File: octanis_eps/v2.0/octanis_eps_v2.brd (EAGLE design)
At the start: 95 x 50 mm, 187 parts, among them Q1 CSD16327Q3_DQG_8, Q2 CSD16327Q3_DQG_8, Q3 CSD16327Q3_DQG_8, Q4 BSS123, Q5 CSD16327Q3_DQG_8, Q6 CSD16327Q3_DQG_8, Q7 BSC0901NS, U1 MSP430FR5969, U10 INA213, U11 MIC5019, U12 TPS61088, U13 TPS61232, U15 Value, U16 Value, U17 Value, U2 OPA2333DGK, U3 TPS2022D, U4 TPS2022D, U5 BQ24650_RVA_16, U7 TPS61232, U9 INA213, X1 32.768kHz

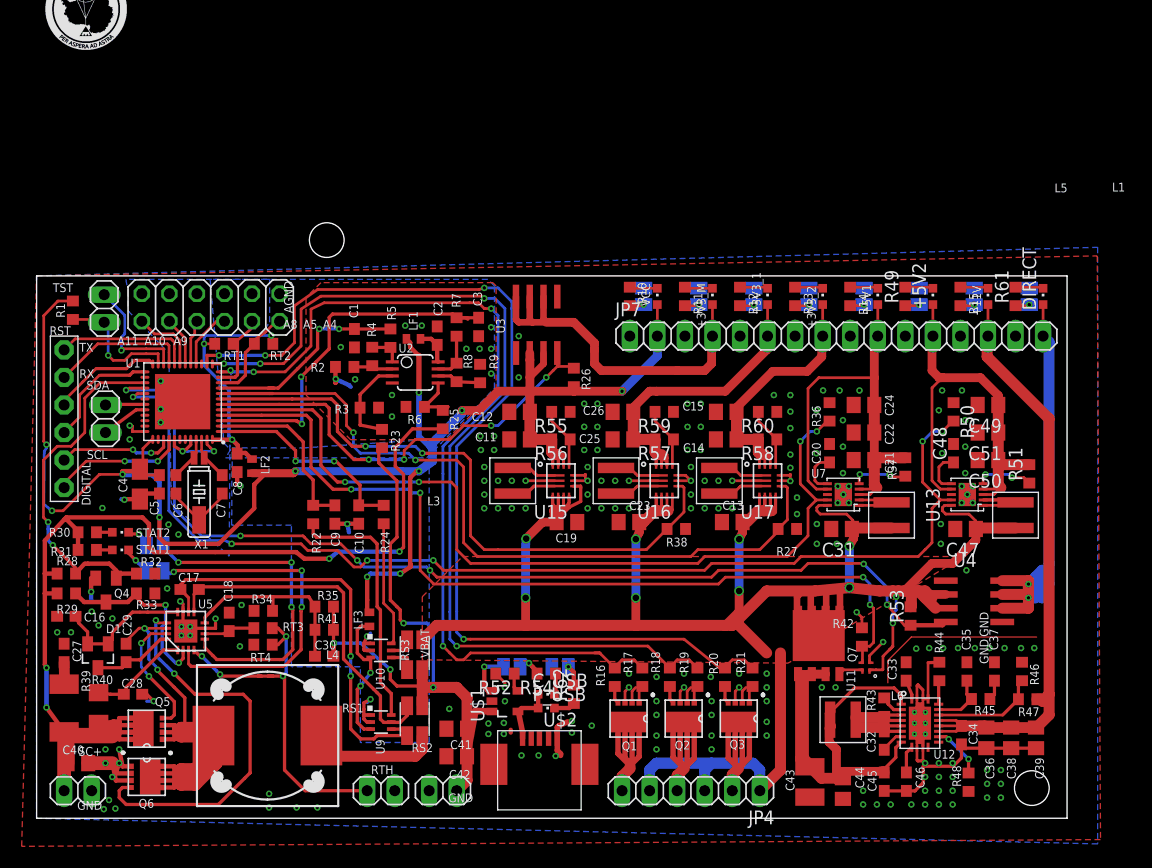
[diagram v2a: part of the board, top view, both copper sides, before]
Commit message: corrected some GND mistakes; finished v2.0 silk layer
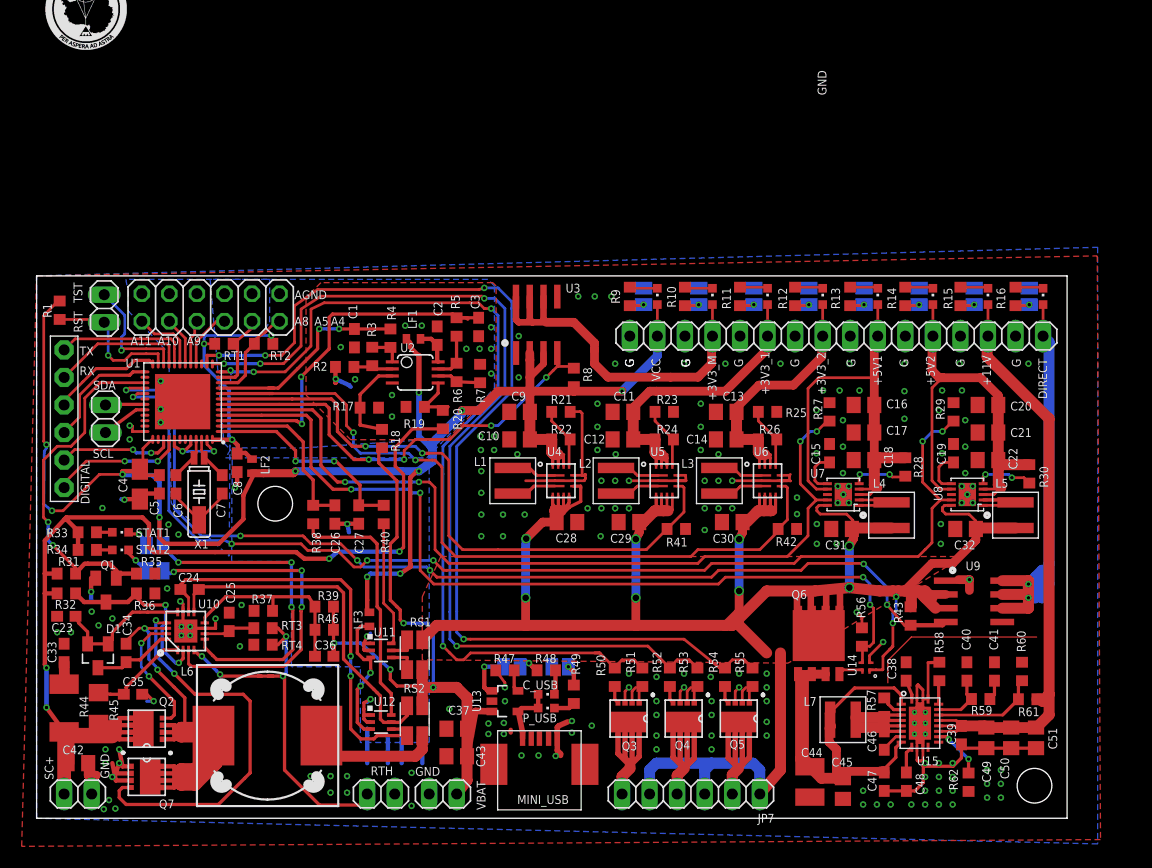
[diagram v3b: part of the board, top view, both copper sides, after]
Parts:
- removed J1, J2, J3, J4: (no value), jumper:SJ
- removed RS3: 10m, Octanis1_EPS:4PADS_RESISTOR
- removed U$1: MCP73831/2, Octanis1_EPS:SOT23-5
- removed U16: Value, octanis_eps_v05:RNC0014A
- added J108, J109, J110, J111: (no value), jumper:SJ
- added RS2: 10m, Octanis1_EPS:4PADS_RESISTOR
- added U14: MIC5019, Octanis1_EPS:QFN-4
- added U8: TPS61232, texasinstruments:S-PVSON-N10
- C10, C9: value 1.5uF -> 22uF; device rcl:C0603 -> resistor:C0805
- C13: value 10uF -> 22uF
- C15: value 22uF -> 10nF; device resistor:C0805 -> rcl:C0603
- C16, C18: value 1uF -> 22uF; device rcl:C0603 -> resistor:C0805
- C17, C32: value 100nF -> 22uF; device rcl:C0603 -> resistor:C0805
- C19: value 10uF -> 10nF; device resistor:C0805 -> rcl:C0603
- C20: value 10nF -> 22uF; device rcl:C0603 -> resistor:C0805
- C23: value 10uF -> 1uF; device resistor:C0805 -> rcl:C0603
- C24, C47: value 22uF -> 100nF; device resistor:C0805 -> rcl:C0603
- C25, C39: value 22uF -> 1uF; device resistor:C0805 -> rcl:C0603
- C26: value 22uF -> 1.5uF; device resistor:C0805 -> rcl:C0603
- C27: value 2.2uF -> 1.5uF
- C28: value 1uF -> 10uF; device rcl:C0603 -> resistor:C0805
- C29, C45: value 100nF -> 10uF; device rcl:C0603 -> resistor:C0805
- C30: value 22pF -> 10uF; device rcl:C0603 -> resistor:C0805
- C34: value 1uF -> 100nF
- C35: value 150pF -> 1uF
- C36: value 22uF -> 22pF; device resistor:C0805 -> rcl:C0603
- C37: value 4.7nF -> 10uF; device rcl:C0603 -> resistor:C0805
- C38: value 22uF -> 2.2uF; device resistor:C0805 -> rcl:C0603
- C40: value 10uF -> 150pF; device resistor:C0805 -> rcl:C0603
- C41: value 10uF -> 4.7nF; device resistor:C0805 -> rcl:C0603
- C43: value 47uF Tantal -> 10uF; device rcl:C1210 -> resistor:C0805
- C44: value 10uF -> 47uF Tantal; device resistor:C0805 -> rcl:C1210
- C46: value 47nF -> 100nF
- C48: value 10nF -> 47nF
- JP3: device Headerlibrary:1X02 -> Headerlibrary:1X16
- JP4: device Headerlibrary:1X06 -> Headerlibrary:1X02
- JP7: device Headerlibrary:1X16 -> Headerlibrary:1X06
- L4: value DR127_6u8 -> 1uH; device inductors:DR127 -> Coilcraft:XFL4020
- L6: value 1.5uH -> DR127_6u8; device Coilcraft:XFL4020 -> inductors:DR127
- L7: value 1uH -> 1.5uH
- Q1: value CSD16327Q3_DQG_8 -> BSS123; device texasinstruments:DQG8 -> transistor-small-signal:SOT23
- Q4: value BSS123 -> CSD16327Q3_DQG_8; device transistor-small-signal:SOT23 -> texasinstruments:DQG8
- Q6: value CSD16327Q3_DQG_8 -> BSC0901NS; device texasinstruments:DQG8 -> transistor-power:PG-TDSON-8
- Q7: value BSC0901NS -> CSD16327Q3_DQG_8; device transistor-power:PG-TDSON-8 -> texasinstruments:DQG8
- R13, R16: value 1k -> 1.5k
- R17, R19: value 1M -> 100k (0.1%)
- R18: value 1k -> 200k (0.1%)
- R20, R7: value 1k -> 330k (0.1%)
- R21: value 1M -> 150k
- R22, R24: value 1k -> 360k
- R23: value 200k (0.1%) -> 150k
- R25: value 330k (0.1%) -> 150k
- R26: value 1M -> 360k; device resistor:R0603 -> rcl:R0603
- R27, R53: device resistor:R0603 -> rcl:R0603
- R28: value dnp -> 1M
- R29: value Rmpph -> 1M
- R30: value 4k7 -> 1M
- R31: value 4k7 -> dnp
- R32: value 1M -> Rmpph
- R33: value Rmppl -> 4k7
- R34: value 100k (1%) -> 4k7
- R35: value 100k (1%) -> 1M
- R36: value 1M -> Rmppl
- R37: value 1M -> 100k (1%)
- R38: value 1M -> 1k; device resistor:R0603 -> rcl:R0603
- R39: value 2 -> 100k (1%); device rcl:R2010 -> rcl:R0603
- R4: value 100k (0.1%) -> 1k
- R40: value 10 -> 1k; device rcl:R1206 -> rcl:R0603
- R41: value 2.2M (1%) -> 1M; device rcl:R0603 -> resistor:R0603
- R42: device rcl:R0603 -> resistor:R0603
- R43: value 47k -> 1M
- R44: value 100k -> 2; device resistor:R0603 -> rcl:R2010
- R45: value 150-220k -> 10; device resistor:R0603 -> rcl:R1206
- R46: value 56k -> 2.2M (1%); device resistor:R0603 -> rcl:R0603
- R47: value 430k -> 2k; device resistor:R0603 -> rcl:R0603
- R48: value dnp -> 470; device resistor:R0603 -> rcl:R0603
- R49: value 1.5k -> 1k
- R50: value 1M -> 1k
- R52: value 2k -> 1k
- R54: value 470 -> 1k
- R55: value 150k -> 1M
- R56: value 360k -> 1M
- R57: value 360k -> 47k; device rcl:R0603 -> resistor:R0603
- R58: value 360k -> 100k; device rcl:R0603 -> resistor:R0603
- R59: value 150k -> 150-220k; device rcl:R0603 -> resistor:R0603
- R60: value 150k -> 56k; device rcl:R0603 -> resistor:R0603
- R61: value 1.5k -> 430k; device rcl:R0603 -> resistor:R0603
- R62: value 1k -> dnp; device rcl:R0603 -> resistor:R0603
- R8: value 100k (0.1%) -> 1M; device rcl:R0603 -> resistor:R0603
- R9: value 330k (0.1%) -> 1k
- U10: value INA213 -> BQ24650_RVA_16; device Octanis1_EPS:SC70-6 -> octanis_eps_v05:RVA16_2P14X2P14
- U11: value MIC5019 -> INA213; device Octanis1_EPS:QFN-4 -> Octanis1_EPS:SC70-6
- U12: value TPS61088 -> INA213; device texasinstruments:R-PVQFN-N20 -> Octanis1_EPS:SC70-6
- U13: value TPS61232 -> MCP73831/2; device texasinstruments:S-PVSON-N10 -> Octanis1_EPS:SOT23-5
- U15: value Value -> TPS61088; device octanis_eps_v05:RNC0014A -> texasinstruments:R-PVQFN-N20
- U4: value TPS2022D -> Value; device Octanis1_EPS:SO8 -> octanis_eps_v05:RNC0014A
- U5: value BQ24650_RVA_16 -> Value; device octanis_eps_v05:RVA16_2P14X2P14 -> octanis_eps_v05:RNC0014A
- U9: value INA213 -> TPS2022D; device Octanis1_EPS:SC70-6 -> Octanis1_EPS:SO8
- moved R30 87.0 mm to (91.5, 31.8), turned to 90 degrees
- moved R29 83.5 mm to (84.5, 37.5), turned to 270 degrees
- moved C40 82.4 mm to (85.8, 13.5), turned to 90 degrees
- moved R45 81.3 mm to (5.71, 10.2), turned to 90 degrees
- moved R44 80.8 mm to (2.54, 10.2)
- moved J102 79.7 mm to (10.9, 22.8), turned to 0 degrees
- moved R28 78.0 mm to (80.1, 32.4), turned to 90 degrees
- moved C33 77.6 mm to (2.54, 15.2)
- moved C34 77.4 mm to (8.26, 15.2), turned to 270 degrees
- moved C35 76.9 mm to (8.89, 11.4), turned to 0 degrees
- moved C16 76.1 mm to (76.3, 38.1)
- moved J103 69.3 mm to (10.9, 25.1), turned to 0 degrees
- moved JP3 67.8 mm to (73.7, 44.5), turned to 0 degrees
- moved R36 65.2 mm to (10.1, 20.7), turned to 180 degrees
- moved C24 64.5 mm to (14.1, 21.1)
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- renumbered U$2 to MINI_USB, U17 to U6
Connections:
- net +12V: now also C49.2, C50.2, C51.2, JP3.14, R61.2, U15.P$14, U15.P$15, U15.P$16; no longer C34.2, C36.2, C38.2, JP7.14, R47.2, U12.P$14, U12.P$15, U12.P$16
- net +3V3: now also C10.1, C9.1, JP3.2, R22.2, R8.2, U4.12, U4.13, U4.14; no longer C11.1, C12.1, JP7.2, R26.2, R56.2, U15.12, U15.13, U15.14
- net +3V3_1: now also C11.1, C12.1, JP3.6, R24.2, U5.12, U5.13, U5.14; no longer C25.1, C26.1, JP7.6, R57.2, U16.12, U16.13, U16.14
- net +3V3_2: now also C13.1, JP3.8, R26.2; no longer C15.1, JP7.8, R58.2
- net +3V3_M: now also JP3.4; no longer JP7.4
- net +5V_1: now also C16.1, C17.1, C18.1, JP3.10, R28.2; no longer C21.1, C22.1, C24.1, JP7.10, R37.2
- net +5V_2: now also C20.1, C21.1, C22.1, JP3.12, R30.2, U8.3, U8.4, U8.7; no longer C49.1, C50.1, C51.1, JP7.12, R51.2, U13.3, U13.4, U13.7
- net AGND: now also C26.1, C27.1, R17.1, R19.1, R7.2, U11.1, U11.2, U12.1, U12.2; no longer C10.1, C9.1, R3.1, R6.1, R9.2, U10.1, U10.2, U9.1, U9.2
- net AVCC1: now also U11.3, U12.3; no longer U10.3, U9.3
- net BAT+: now also C36.1, C37.1, C43.1, R18.2, R39.2, R46.2, RS1.I1, RS2.I2, U13.3; no longer C30.1, C41.1, C42.1, R23.2, R35.2, R41.2, RS1.I2, RS3.I1, U$1.3
- net BAT_11V: now also C47.1, L7.P$1, Q6.1, Q6.2, Q6.3, U15.P$2, U15.P$9; no longer C43.1, L6.P$1, Q7.1, Q7.2, Q7.3, U12.P$2, U12.P$9
- net BAT_OUT: now also C28.1, C29.1, C30.1, C32.1, JP7.1, JP7.3, JP7.5, L4.P$1, Q6.5, Q6.6, Q6.7, Q6.8, R43.2, RS1.I2, U14.P$1, U14.P1, U4.4, U4.5, U4.6, U4.7, U4.8, U5.4, U5.5, U5.6, U5.7, U8.10, U9.2, U9.3; no longer C13.1, C19.1, C23.1, C47.1, JP4.1, JP4.3, JP4.5, L7.P$1, Q7.5, Q7.6, Q7.7, Q7.8, R53.2, RS3.I2, U11.P$1, U11.P1, U13.10, U15.4, U15.5, U15.6, U15.7, U15.8, U16.4, U16.5, U16.6, U16.7, U4.2, U4.3
- net DIRECT: now also JP3.16, U9.6, U9.7, U9.8; no longer JP7.16, U4.6, U4.7, U4.8
- net EN_12V: now also R56.2, U14.P$3, U14.P3; no longer R42.2, U11.P$3, U11.P3
- net EN_3V3_1: now also R41.1, U5.8; no longer R38.1, U16.8
- net EN_3V3_2: now also R42.1; no longer R27.1
- net EN_3V3_M: now also R8.1; no longer R26.1
- net EN_5V_1: now also R27.2; no longer R36.2
- net EN_5V_2: now also R29.2, U8.9; no longer R50.2, U13.9
- net EN_DIRECT: now also R43.1, U9.4; no longer R53.1, U4.4
- net EN_HEAT1: now also R50.2, R51.1; no longer R16.2, R17.1
- net EN_HEAT2: now also R52.2, R53.1; no longer R18.2, R19.1
- net EN_HEAT3: now also R54.2, R55.1; no longer R20.2, R21.1
- net EN_SC: now also Q1.1, R31.1, R35.2; no longer Q4.1, R28.1, R32.2
- net GND: now also C10.2, C17.2, C29.2, C30.2, C32.2, C38.2, C40.2, C42.1, C49.1, C50.1, C51.1, C9.2, J100.2, J108.1, J109.1, J110.1, J111.1, JP3.1, JP3.11, JP3.13, JP3.15, JP3.3, JP3.5, JP3.7, JP3.9, Q4.1, Q4.3, Q5.1, Q5.2, Q5.3, Q7.1, Q7.2, Q7.3, R21.1, R23.1, R25.1, R27.1, R29.1, R35.1, R37.1, R41.2, R42.2, R47.2, R51.2, R53.2, R55.2, R56.1, R58.1, R62.2, U10.11, U10.17, U10.7, U10.V, U10.V_1, U10.V_2, U10.V_3, U13.2, U14.P$2, U14.P2, U15.P$20, U15.PGND1, U15.PGND10, U15.PGND11, U15.PGND12, U15.PGND2, U15.PGND3, U15.PGND4, U15.PGND5, U15.PGND6, U15.PGND7, U15.PGND8, U15.PGND9, U4.10, U4.2, U4.9, U5.10, U5.2, U5.9, U8.EXPAD, U8.GND1, U8.GND2, U8.GND3, U8.GND4, U8.GND5, U9.1; no longer C24.2, C26.2, C27.2, C34.1, C36.1, C38.1, C40.1, C42.2, C46.2, C49.2, C50.2, C51.2, J1.1, J102.1, J103.1, J3.1, J4.2, JP7.1, JP7.11, JP7.13, JP7.15, JP7.3, JP7.5, JP7.7, JP7.9, Q1.1, Q1.3, Q2.1, Q2.2, Q2.3, Q6.1, Q6.2, Q6.3, R17.2, R19.2, R21.2, R27.2, R32.1, R33.1, R34.1, R38.2, R42.1, R44.1, R46.1, R48.2, R50.1, R52.2, R55.1, R59.1, U$1.2, U11.P$2, U11.P2, U12.P$20, U12.PGND1, U12.PGND10, U12.PGND11, U12.PGND12, U12.PGND2, U12.PGND3, U12.PGND4, U12.PGND5, U12.PGND6, U12.PGND7, U12.PGND8, U12.PGND9, U13.EXPAD, U13.GND1, U13.GND2, U13.GND3, U13.GND4, U13.GND5, U15.10, U15.2, U15.9, U16.10, U16.2, U16.9, U4.1, U5.11, U5.17, U5.7, U5.V, U5.V_1, U5.V_2, U5.V_3
- net HEAT1: now also JP7.6, Q3.5, Q3.6, Q3.7, Q3.8; no longer JP4.6, Q1.5, Q1.6, Q1.7, Q1.8
- net HEAT2: now also JP7.4, Q4.5, Q4.6, Q4.7, Q4.8; no longer JP4.4, Q2.5, Q2.6, Q2.7, Q2.8
- net HEAT3: now also JP7.2, Q5.5, Q5.6, Q5.7, Q5.8; no longer JP4.2, Q3.5, Q3.6, Q3.7, Q3.8
- net I2C_SCL: now also JP4.2; no longer JP3.2
- net I2C_SDA: now also JP4.1; no longer JP3.1
- net IND: now also L4.P$2; no longer L5.P$2
- net IND1: now also L5.P$2, U8.1, U8.2; no longer L7.P$2, U13.1, U13.2
- net I_IN: now also C26.2, R38.1; no longer C9.2, R22.1
- net I_OUT: now also C27.2, R40.1; no longer C10.2, R24.1
- net LED1: now also R14.2; no longer R49.2
- net LED2: now also R16.2; no longer R61.2
- net LED5: now also R13.2; no longer R14.2
- net N$1: now also L1.P$1, U4.3; no longer L3.P$1, U15.3
- net N$10: now also Q6.4, U14.P$4, U14.P4; no longer Q7.4, U11.P$4, U11.P4
- net N$11: now also L3.P$1; no longer L1.P$1
- net N$12: now also L3.P$2; no longer L1.P$2
- net N$14: now also J107.2, R13.1; no longer J103.2, R14.1
- net N$19: now also R3.1, R4.2; no longer R4.1, R5.2
- net N$2: now also R28.1; no longer R37.1
- net N$20: now also R3.2; no longer R4.2
- net N$21: now also R17.2, R18.1; no longer R23.1, R3.2
- net N$22: now also R5.2, R6.1; no longer R7.2, R8.1
- net N$23: now also R6.2, R7.1; no longer R8.2, R9.1
- net N$24: now also R19.2, R20.1; no longer R25.1, R6.2
- net N$25: now also R40.2, U11.6; no longer R24.2, U10.6
- net N$26: now also R38.2, U12.6; no longer R22.2, U9.6
- net N$27: now also Q5.4, R54.1; no longer Q3.4, R20.1
- net N$3: now also L1.P$2, U4.1; no longer L3.P$2, U15.1
- net N$31: now also Q4.4, R52.1; no longer Q2.4, R18.1
- net N$32: now also RS1.V1, U11.4; no longer RS3.V1, U10.4
- net N$33: now also RS1.V2, U11.5; no longer RS3.V2, U10.5
- net N$34: now also R21.2, R22.1, U4.11; no longer R55.2, R56.1, U15.11
- net N$35: now also R23.2, R24.1, U5.11; no longer R57.1, R59.2, U16.11
- net N$37: now also Q3.4, R50.1; no longer Q1.4, R16.1
- net N$38: now also C46.2, U15.P$8; no longer C32.2, U12.P$8
- net N$39: now also R10.2; no longer R11.2
- net N$4: now also L6.2, RS2.I1; no longer L4.2, RS1.I1
- net N$40: now also J110.2, R10.1; no longer J106.2, R11.1
- net N$42: now also C33.1, R44.1; no longer C27.1, R39.1
- net N$43: now also R9.2; no longer R10.2
- net N$44: now also R30.1, U8.5; no longer R51.1, U13.5
- net N$45: now also J111.2, R9.1; no longer J107.2, R10.1
- net N$46: now also R12.2; no longer R13.2
- net N$47: now also J108.2, R12.1; no longer J104.2, R13.1
- net N$49: now also J105.2; no longer J102.2
- net N$5: now also C15.1; no longer C20.1
- net N$50: now also C46.1, L7.P$2, R57.2, U15.P$4, U15.P$5, U15.P$6, U15.P$7; no longer C32.1, L6.P$2, R43.2, U12.P$4, U12.P$5, U12.P$6, U12.P$7
- net N$51: now also R11.2; no longer R12.2
- net N$52: now also J109.2, R11.1; no longer J105.2, R12.1
- net N$53: now also R57.1, U15.P$3; no longer R43.1, U12.P$3
- net N$54: now also C41.1, R59.1; no longer C37.1, R45.1
- net N$55: now also J106.2, R14.1; no longer J1.2, R49.1
- net N$56: now also C48.1, U15.P$10; no longer C46.1, U12.P$10
- net N$57: now also R58.2, U15.P$19; no longer R44.2, U12.P$19
- net N$58: now also C40.1, R59.2, U15.P$18; no longer C35.1, R45.2, U12.P$18
- net N$59: now also C38.1, U15.P$1; no longer C33.1, U12.P$1
- net N$6: now also U5.3; no longer U16.3
- net N$60: now also R60.2, R61.1, U15.P$17; no longer R46.2, R47.1, U12.P$17
- net N$61: now also C19.1, U8.6; no longer C48.1, U13.6
- net N$62: now also R25.2, R26.1; no longer R58.1, R60.2
- net N$63: now also R47.1, U13.5; no longer R52.1, U$1.5
- net N$64: now also Q1.3, R32.1, R36.2, U10.2; no longer Q4.3, R29.1, R33.2, U5.2
- net N$65: now also J101.1, U13.1; no longer J2.1, U$1.1
- net N$66: now also R34.1, STAT2.A; no longer R31.1, STAT1.A
- net N$67: now also J103.2, STAT1.C; no longer J101.2, STAT2.C
- net N$68: now also J102.2, STAT2.C; no longer J100.2, STAT1.C
- net N$69: now also R33.1, STAT1.A; no longer R30.1, STAT2.A
- net N$7: now also U5.1; no longer U16.1
- net N$70: now also J103.1, U10.5; no longer J101.1, U5.5
- net N$71: now also J102.1, U10.3; no longer J100.1, U5.3
- net N$72: now also C25.1, U10.6; no longer C18.1, U5.6
- net N$73: now also C35.1, R45.2, U10.1; no longer C28.1, R40.2, U5.1
- net N$74: now also J101.2, R48.2; no longer J2.2, R54.2
- net N$75: now also R48.1; no longer R54.1
- net N$76: now also C34.1, L6.1, Q2.1, Q2.2, Q2.3, Q7.5, Q7.6, Q7.7, Q7.8, U10.14; no longer C29.1, L4.1, Q5.1, Q5.2, Q5.3, Q6.5, Q6.6, Q6.7, Q6.8, U5.14
- net N$77: now also J104.2, R16.1; no longer J3.2, R61.1
- net N$78: now also R49.1; no longer R62.1
- net N$79: now also J100.1, R49.2; no longer J4.1, R62.2
- net N$80: now also Q2.4, U10.15; no longer Q5.4, U5.15
- net N$81: now also Q7.4, U10.13; no longer Q6.4, U5.13
- net N$82: now also C36.2, R37.2, R39.1, R46.1, U10.8; no longer C30.2, R34.2, R35.1, R41.1, U5.8
- net N$84: now also C23.1, U10.12; no longer C16.1, U5.12
- net N$85: now also C34.2, U10.16; no longer C29.2, U5.16
- net N$9: now also R62.1, U15.P$13; no longer R48.1, U12.P$13
- net SC+: now also C42.2, Q2.5, Q2.6, Q2.7, Q2.8, R20.2, R32.2, R33.2, R34.2, R44.2, R45.1; no longer C40.2, Q5.5, Q5.6, Q5.7, Q5.8, R25.2, R28.2, R29.2, R30.2, R39.2, R40.1
- net TS: now also U10.4; no longer U5.4
- net V_BAT: now also R4.1; no longer R5.1
- net V_BAT+: now also C24.1, RS2.V2, U10.9, U12.5; no longer C17.1, RS1.V2, U5.9, U9.5
- net V_SC: now also R5.1; no longer R7.1
- net V_SCOUT: now also C24.2, RS2.V1, U10.10, U12.4; no longer C17.2, RS1.V1, U5.10, U9.4
- net V_USB: now also U13.4; no longer U$1.4
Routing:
- net GND: track 112.4 -> 136.7 mm, vias 181 -> 168
- net AGND: track 23.3 -> 26.5 mm
- net TS: track 34.5 -> 36.0 mm
- net N$13: track 12.2 -> 13.4 mm
- net BAT_OUT: track 230.4 -> 231.6 mm
- net +3V3: track 168.8 -> 167.6 mm
- net +3V3_M: track 33.9 -> 34.4 mm
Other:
- board text added: "G"
- board text added: "L2"
- board text added: "L4"
- board text added: "L7"
- board text removed: "L6"
- board text removed: "RS3"

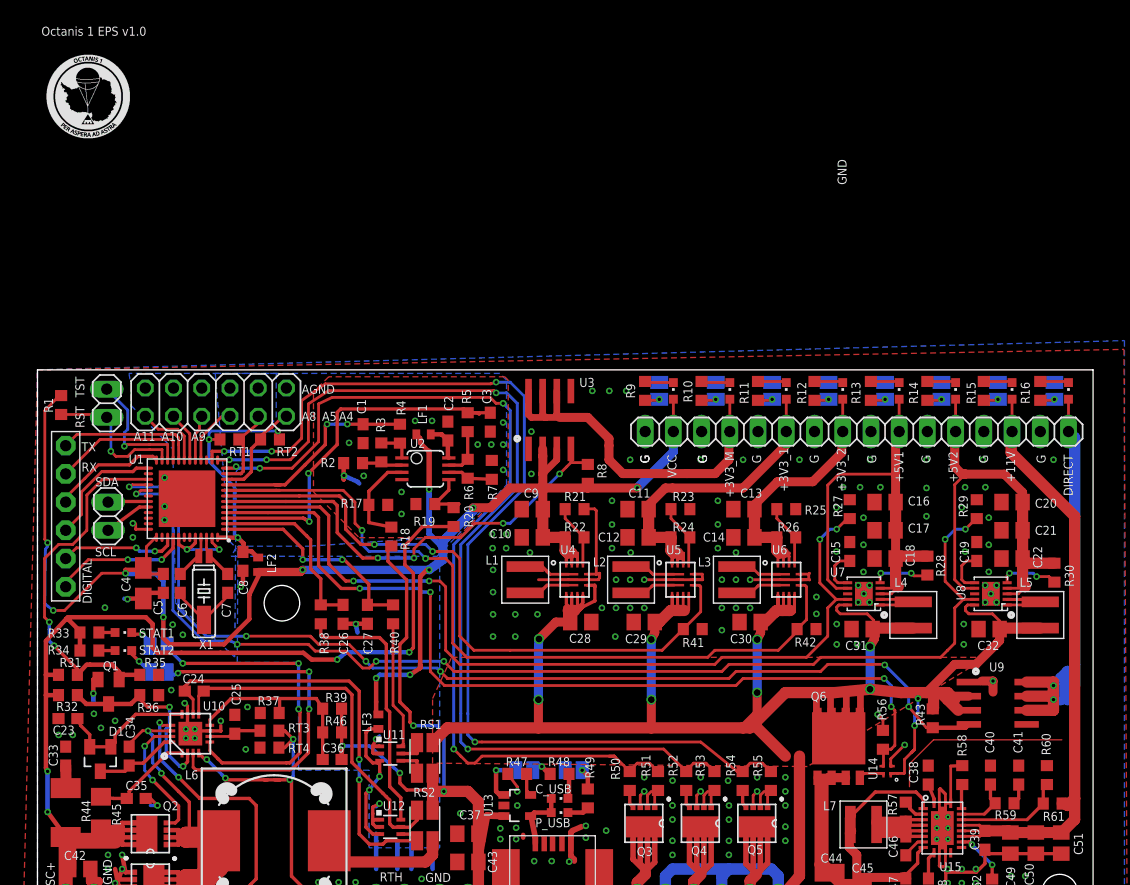
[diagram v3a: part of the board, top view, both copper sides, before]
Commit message: updated titles and moved logo
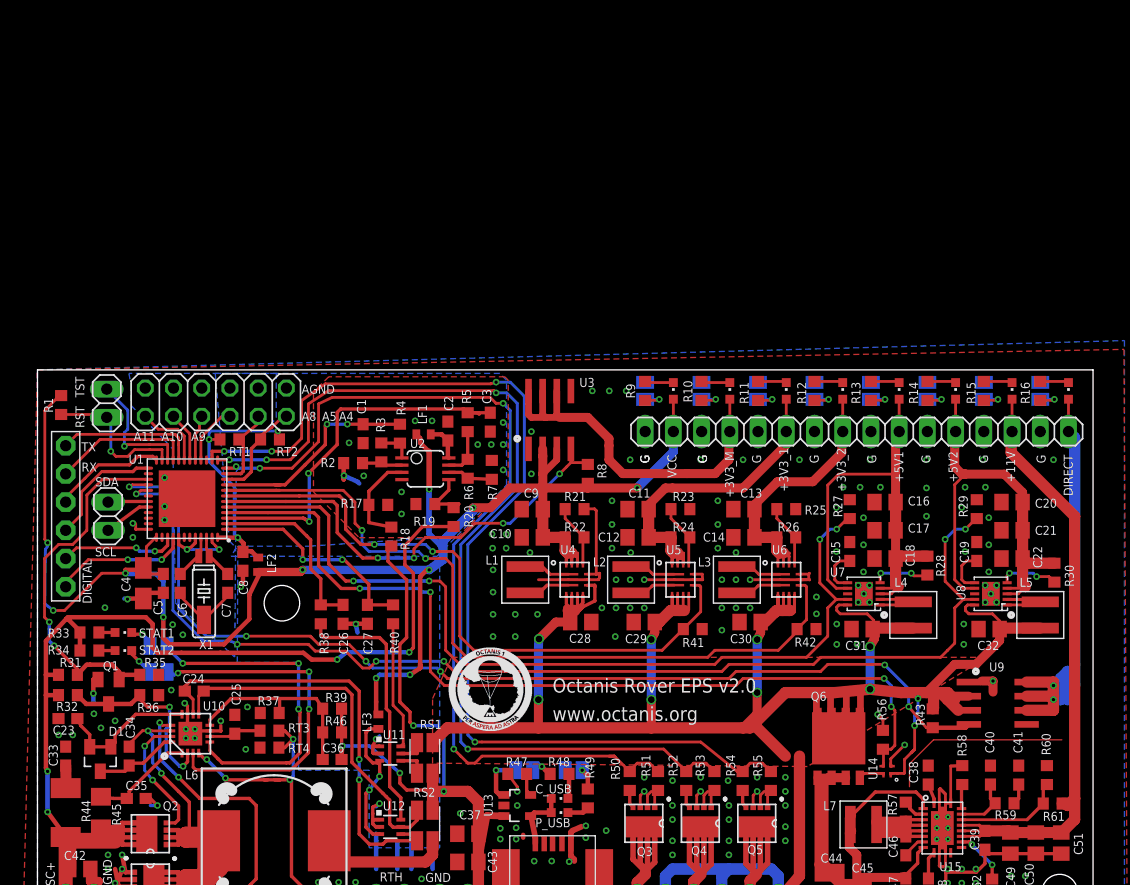
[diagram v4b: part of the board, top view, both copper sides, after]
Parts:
- moved J109 1.27 mm to (64.8, 48.1)
- moved J111 1.27 mm to (54.7, 48.1)
- moved J104 1.27 mm to (90.2, 48.1)
- moved J105 1.27 mm to (85.2, 48.1)
- moved J106 1.27 mm to (80.1, 48.1)
- moved J107 1.27 mm to (75.0, 48.1)
- moved J108 1.27 mm to (69.9, 48.1)
- moved J110 1.27 mm to (59.8, 48.1)
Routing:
- net N$14: track 1.91 -> 4.23 mm
- net N$47: track 1.91 -> 4.23 mm
- net N$77: track 1.91 -> 3.94 mm
- net GND: track 136.7 -> 138.6 mm
- net N$55: track 1.91 -> 3.52 mm
- net N$52: track 1.91 -> 3.35 mm
- net N$49: track 1.91 -> 3.32 mm
- net N$45: track 1.91 -> 3.05 mm
- net N$40: track 1.91 -> 3.05 mm
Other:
- board text added: "BAT_H3_BAT_H2_BAT_H1"
- board text added: "BAT__G___G__RTBAT"
- board text added: "DIR__G___11__G__5.2__G__5.1__G__3.2__G___3.1__G__3M__G_VCC__G"
- board text added: "G__SC+"
- board text added: "Octanis Rover EPS v2.0"
- board text removed: "Octanis 1 EPS v1.0"

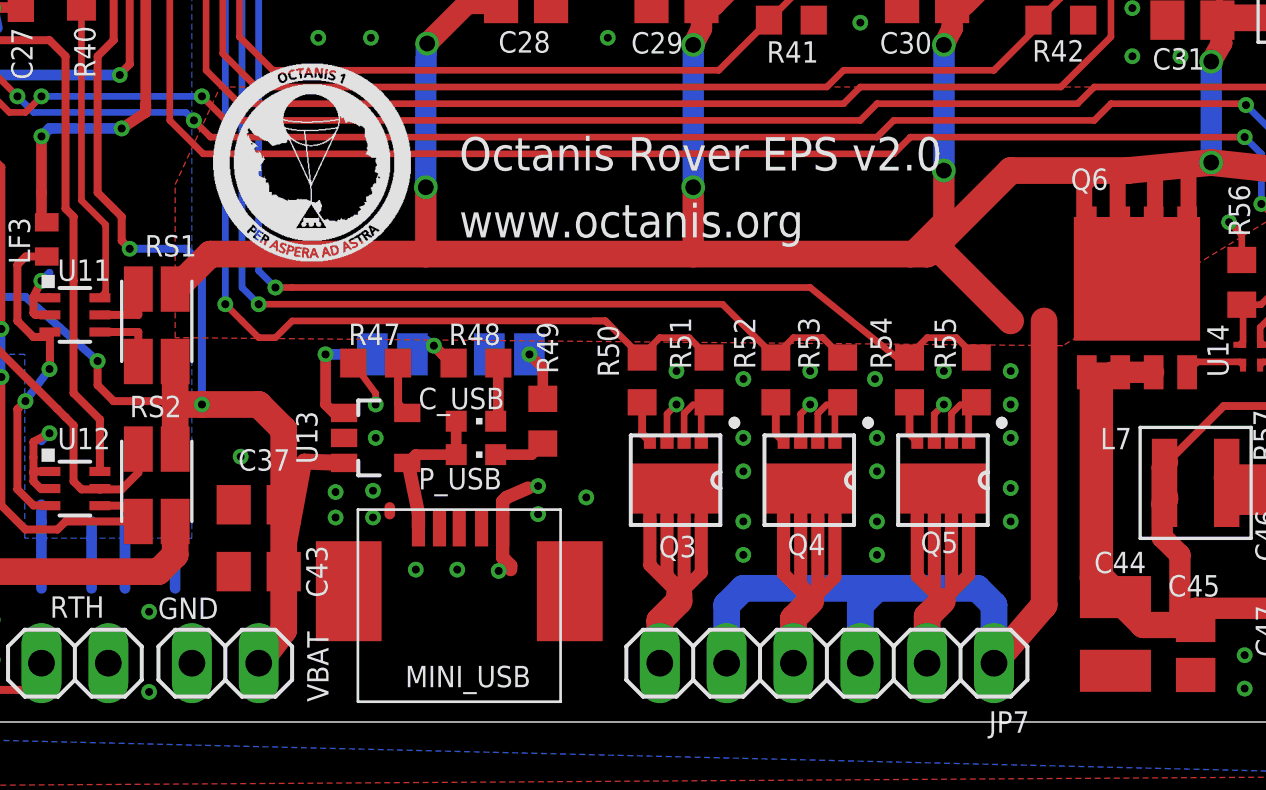
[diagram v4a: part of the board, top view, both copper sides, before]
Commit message: finalized silkscreen, generated Gerber files for EPS v2; replaced UV sensor in weather board, generated gerber files for v4
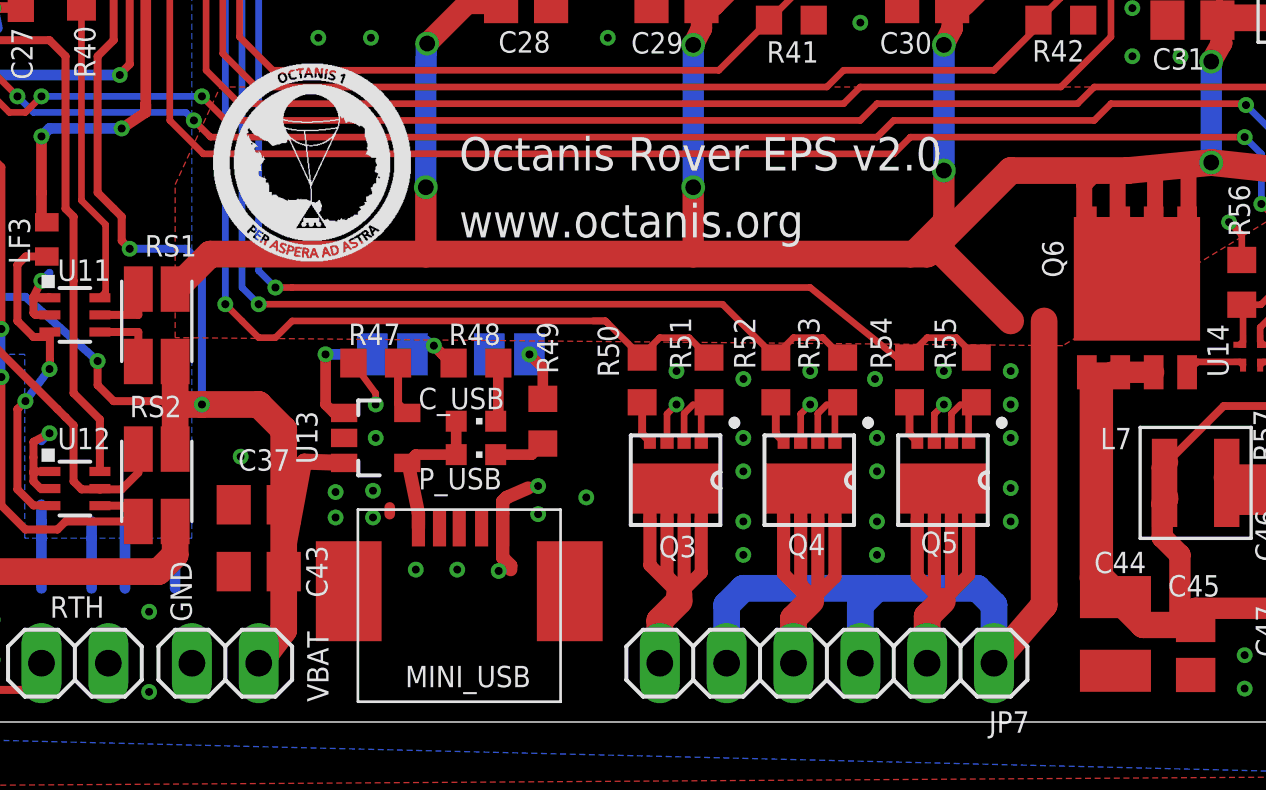
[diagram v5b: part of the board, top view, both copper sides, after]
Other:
- board text added: "BAT G G RTBAT"
- board text added: "BAT H3 BAT H2 BAT H1"
- board text added: "DIR G 11 G 5.2 G 5.1 G 3.2 G 3.1 G 3M G VCC G"
- board text added: "G SC+"
- board text removed: "BAT_H3_BAT_H2_BAT_H1"
- board text removed: "BAT__G___G__RTBAT"
- board text removed: "DIR__G___11__G__5.2__G__5.1__G__3.2__G___3.1__G__3M__G_VCC__G"
- board text removed: "G__SC+"
